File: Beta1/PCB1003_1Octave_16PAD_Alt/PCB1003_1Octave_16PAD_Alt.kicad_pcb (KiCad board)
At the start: 2 copper layers, 188.9 x 64 mm, 101 parts, among them U1 CPT112S, U100 CPT112S, U200 CPT112S

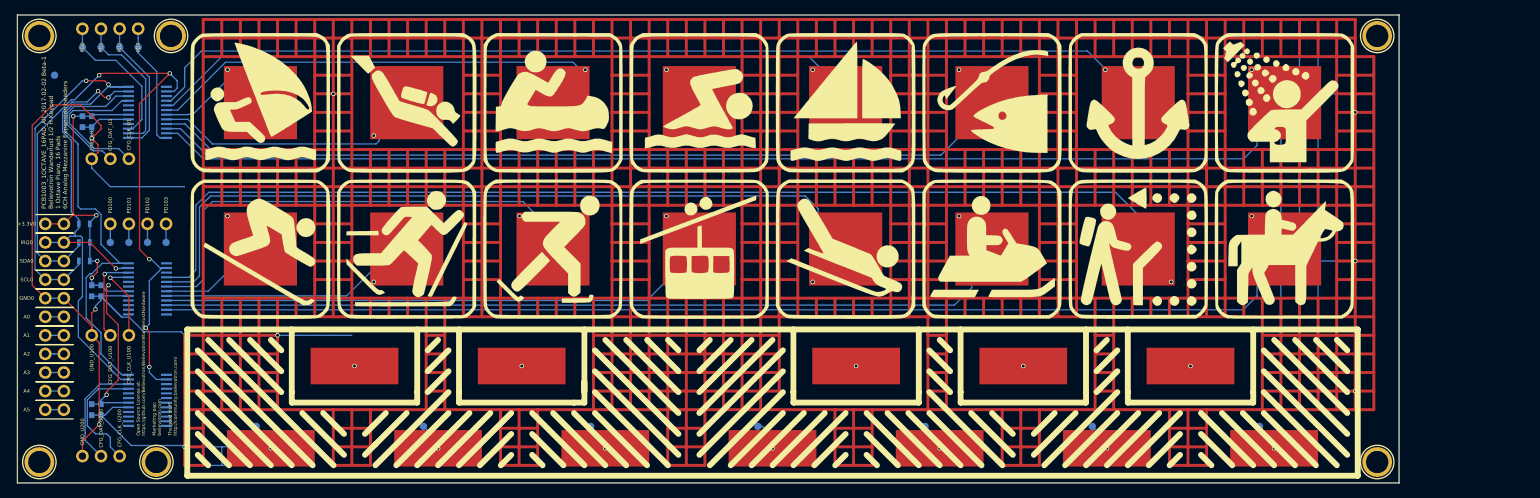
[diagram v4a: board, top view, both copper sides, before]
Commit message: Reroute WIP; Pads are off-screen
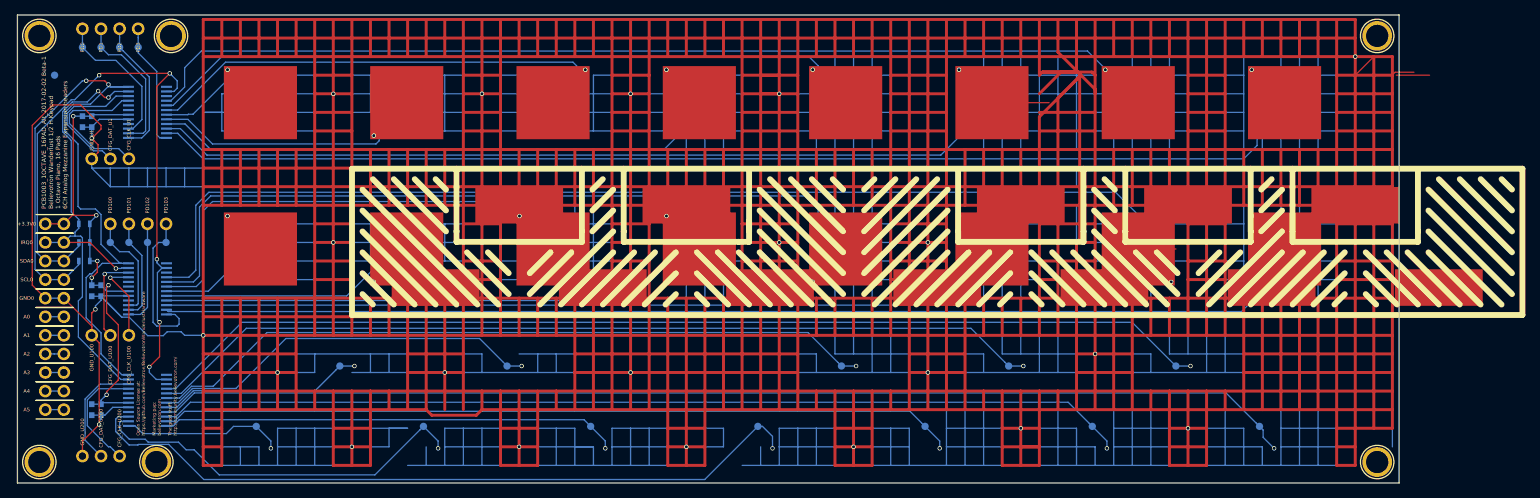
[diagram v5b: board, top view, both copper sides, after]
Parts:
- removed G***: LOGO, Liberry:Adventure_Icons_8x2_160x40
- moved UKEY0 31.5 mm to (48.3, -23.1)
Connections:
- TP103 pad 1: Net-(P111-Pad1) -> Net-(PD103-Pad1)
- UKEY0 pad 1: /CHIP_200 -> /CHIP_202
- UKEY0 pad 10: /CHIP_209 -> /CHIP_205
- UKEY0 pad 11: /CHIP_210 -> /CHIP_211
- UKEY0 pad 12: /CHIP_211 -> /CHIP_206
- UKEY0 pad 2: /CHIP_201 -> /CHIP_207
- UKEY0 pad 3: /CHIP_202 -> /CHIP_201
- UKEY0 pad 4: /CHIP_203 -> /CHIP_208
- UKEY0 pad 5: /CHIP_204 -> /CHIP_203
- UKEY0 pad 6: /CHIP_205 -> /CHIP_200
- UKEY0 pad 7: /CHIP_206 -> /CHIP_209
- UKEY0 pad 8: /CHIP_207 -> /CHIP_204
- UKEY0 pad 9: /CHIP_208 -> /CHIP_210
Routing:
- net GND: track 3440.4 -> 10710.2 mm, vias 5 -> 28
- net (no net): track 1841.5 -> 40.1 mm, vias 4 -> 0
- net /CHIP_206: track 0.00 -> 156.2 mm
- net /CHIP_211: track 2.00 -> 146.2 mm
- net /CHIP_205: track 2.83 -> 132.6 mm
- net /CHIP_210: track 2.00 -> 123.0 mm
- net /CHIP_204: track 3.83 -> 108.9 mm
- net /CHIP_200: track 5.20 -> 101.4 mm
- net /CHIP_209: track 3.71 -> 99.9 mm
- net /CHIP_203: track 2.83 -> 62.5 mm
- net /CHIP_208: track 2.00 -> 53.7 mm
- net /CHIP_201: track 2.83 -> 52.9 mm
- net /CHIP_207: track 3.00 -> 28.0 mm
- net Net-(PD103-Pad1): track 2.54 -> 21.4 mm
- net /CHIP_202: track 3.83 -> 22.1 mm
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
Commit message: Ready for fab.
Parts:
- added G***: LOGO, Liberry:Adventure_Icons_8x2_160x40, F.Cu at (105.8, -42.1)
- moved UKEY0 31.5 mm to (25.8, -1.12)
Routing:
- net GND: track 10710.2 -> 9573.3 mm, vias 28 -> 23
- net (no net): track 40.1 -> 1033.8 mm, vias 0 -> 3
- net /CHIP_05: track 128.5 -> 120.7 mm
- net /CHIP_111: track 160.8 -> 155.7 mm
- net /CHIP_200: track 101.4 -> 99.7 mm
- net /CHIP_202: track 22.1 -> 20.6 mm
- net /CHIP_203: track 62.5 -> 61.0 mm
- net /CHIP_204: track 108.9 -> 107.4 mm
- net /CHIP_205: track 132.6 -> 131.1 mm
- net /CHIP_206: track 156.2 -> 154.7 mm
- net /CHIP_201: track 52.9 -> 51.7 mm
- net /SDA: track 95.6 -> 96.3 mm
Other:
- board text added: "PCB1003_1OCTAVE_16PAD_Alt_2017-03-01 Beta-1 Believotron Wanderlust 1/2 H Keypad 1 Octave Piano, 16 Pads 6CH Analog Mezzanine Expansion headers"
- board text added: "TP show which bit each pad is. Example: TP4 is Bit 4. TP211 is chip 200, bit 11"
- board text removed: "PCB1003_1OCTAVE_16PAD_Alt_2017-02-02 Beta-1 Believotron Wanderlust 1/2 H Keypad 1 Octave Piano, 16 Pads 6CH Analog Mezzanine Expansion headers"
